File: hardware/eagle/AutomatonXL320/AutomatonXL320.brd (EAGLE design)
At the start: 51.8 x 44.2 mm, 46 parts, among them J1 USB_RCPT_10118192-0001LF, J2 ESP_ROBOT_BOARD_GPIO_16, J6 BATTERY, U1 ESP-WROOM-32D, U2 CP2102N-A02-GQFN20, U3 TPS62143RGTT, U4 TXB0106PWRPW16-L, U5 NC7WZ241K8X, U7 TPS62056DGSRDGS10-M

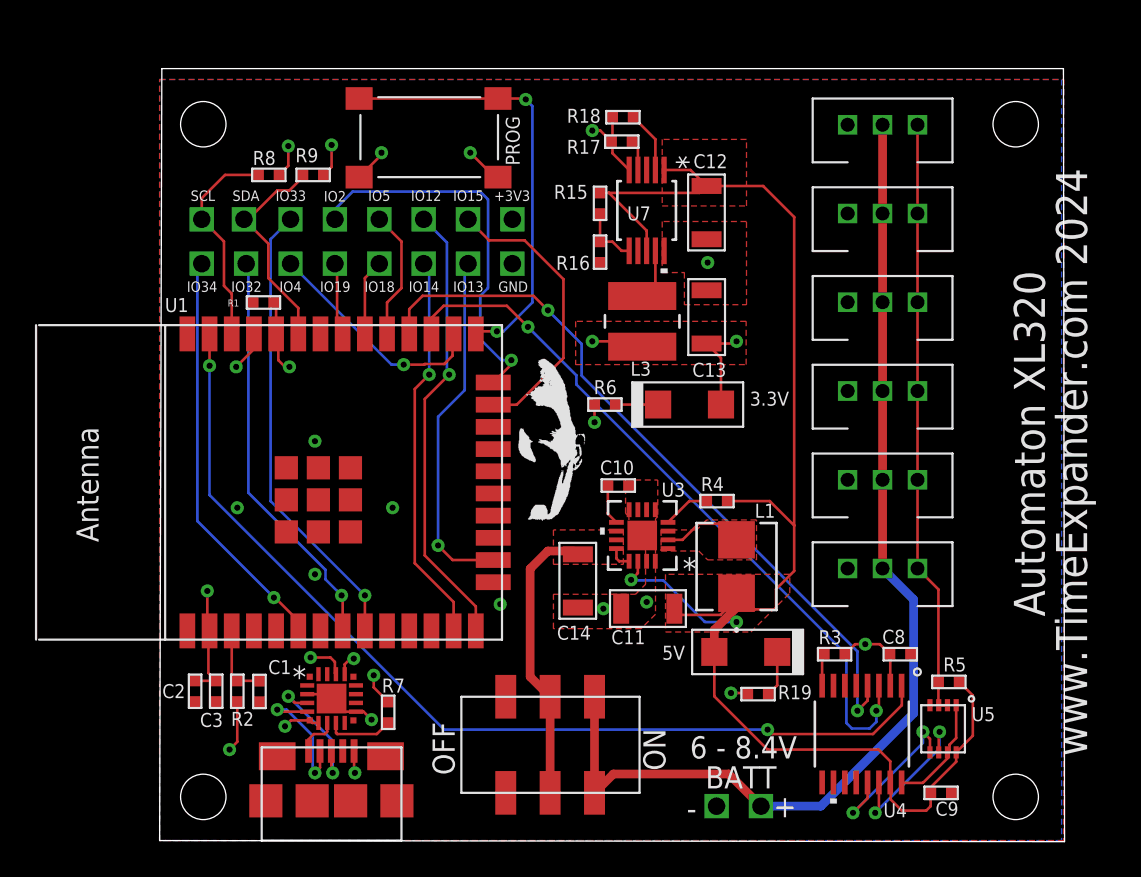
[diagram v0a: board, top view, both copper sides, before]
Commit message: CP2102N VBUS is now connected via resistor ladder
* CP2102N was overheating at times because it was
  connected directly to USB VBUS
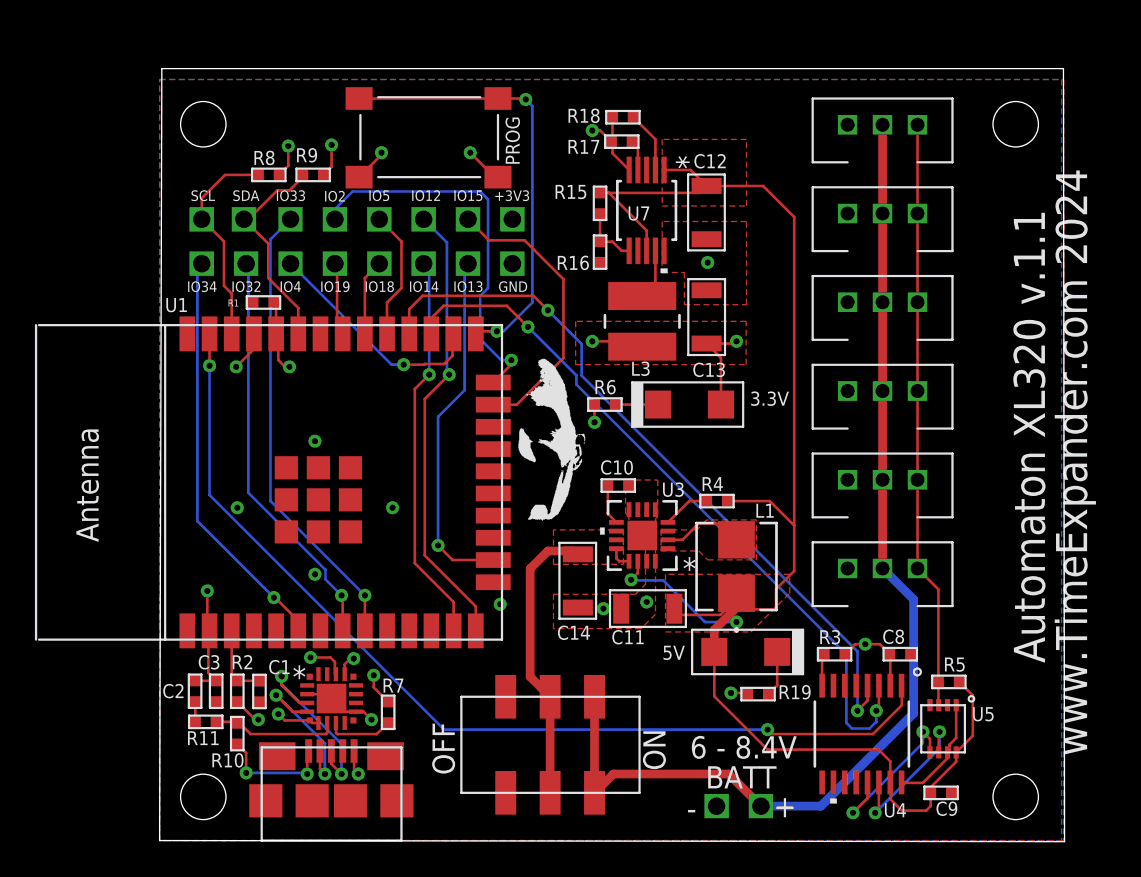
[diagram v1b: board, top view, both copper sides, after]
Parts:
- added R10: 22.1k, TimeExpander2:RES_0402
- added R11: 47.5k, TimeExpander2:RES_0402
- R1, R2, R3, R5, R8, R9: value 10k -> (none)
- R15: value 130k -> (none)
- R16, R4: value 100k -> (none)
- R17, R18: value 1M -> (none)
- R7: value 1k -> (none)
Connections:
- new net N$18: R10.P$2, R11.P$1, U2.8
- net GND: now also R11.P$2
- net N$15: now also R10.P$1; no longer U2.8
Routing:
- net N$18: track 0.00 -> 7.24 mm
- net N$15: track 2.42 -> 6.73 mm, vias 0 -> 2
- net N$16: track 7.96 -> 11.0 mm
- net N$17: track 7.97 -> 9.29 mm
- net GND: track 11.6 -> 13.0 mm
- net 3V3: track 36.3 -> 35.4 mm
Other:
- board text added: "Automaton XL320 v.1.1"
- board text removed: "Automaton XL320"
